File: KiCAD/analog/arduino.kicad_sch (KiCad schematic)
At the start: 53 parts, among them J12 Screw_Terminal_01x04, J13 Screw_Terminal_01x03, J14 Screw_Terminal_01x05, J17 Conn_Coaxial_Small, J18 Conn_Coaxial_Small, J19 Conn_Coaxial_Small, J20 Screw_Terminal_01x04, J21 Screw_Terminal_01x02, J22 Screw_Terminal_01x04, J23 Conn_Coaxial_Small, J24 Conn_Coaxial_Small, J29 Conn_Coaxial_Small, J3 Screw_Terminal_01x04, J30 Conn_Coaxial_Small, J31 8P8C_Shielded, J32 Screw_Terminal_01x02, J6 Screw_Terminal_01x02, J7 Screw_Terminal_01x02, J8 Screw_Terminal_01x02, J9 Screw_Terminal_01x02, Q10 2N7000, Q4 2N7000, Q5 2N7000, Q6 2N7000, Q7 2N7000, U17 Adafruit_PCF8575_Breakout, U18 CD14538B, U3 MCP4728

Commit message: KiCad revC: analog R6 -> 0R jumper (ENC_INT line)
Protoshield already has R7 (330R) + R8 (10K pullup) at the Metro
GPIO input, which is the right place for ESD/noise conditioning
(closest to the sensitive pin). R6 on analog was a duplicate series
resistor on the same signal; dropping it to 0R turns it into an
in-the-path jumper without having to rename the ENC_INT_CLEAN /
ENC_INT labels on multiple sheets.

Co-Authored-By: Claude Opus 4.7 <noreply@anthropic.com>
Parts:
- removed C7: 100nF, Capacitor_THT:C_Disc_D5.0mm_W2.5mm_P5.00mm, symbol Device:C_US
- removed R7: 10K, Resistor_THT:R_Axial_DIN0207_L6.3mm_D2.5mm_P10.16mm_Horizontal, symbol Device:R_US
- R6: value 330R -> 0R

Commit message: revC: accumulated schematic/netlist updates + BOM tooling
- analog + ss_pa netlists regenerated to current schematic state
- interface/arduino/dac/power sheet updates on analog
- fault_shutdown and pa_stage edits on ss_pa (footprint assignments)
- assign_cap_footprints.py: additional VALUE_TO_FOOTPRINT entries
- gen_board_boms.py: per-board BOM generator (multi-sheet .xlsx by
  component category, first-match-wins bucketing, DNP exclusion)
- gen_total_bom.py: consolidated BOM across analog + frontpanel + ss_pa
  for a single Mouser order, board-prefixed references, mixed-footprint
  flagging per Value row

Co-Authored-By: Claude Opus 4.7 <noreply@anthropic.com>
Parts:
- J3: footprint (none) -> TerminalBlock_Phoenix:TerminalBlock_Phoenix_MKDS-1,5-4_1x04_P5.00mm_Horizontal
- J32: footprint (none) -> TerminalBlock_Phoenix:TerminalBlock_Phoenix_MKDS-1,5-2_1x02_P5.00mm_Horizontal
- R12: footprint (none) -> Resistor_THT:R_Axial_DIN0207_L6.3mm_D2.5mm_P10.16mm_Horizontal
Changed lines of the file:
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@@
 			)
 		)
-		(property "Footprint" ""
+		(property "Footprint" "Resistor_THT:R_Axial_DIN0207_L6.3mm_D2.5mm_P10.16mm_Horizontal"
 			(at 207.264 143.764 90)
 			(hide yes)
@@
 			)
 		)
-		(property "Footprint" ""
+		(property "Footprint" "TerminalBlock_Phoenix:TerminalBlock_Phoenix_MKDS-1,5-4_1x04_P5.00mm_Horizontal"
 			(at 24.13 133.35 0)
 			(hide yes)
@@
 			)
 		)
-		(property "Footprint" ""
+		(property "Footprint" "TerminalBlock_Phoenix:TerminalBlock_Phoenix_MKDS-1,5-2_1x02_P5.00mm_Horizontal"
 			(at 215.9 147.32 0)
 			(hide yes)

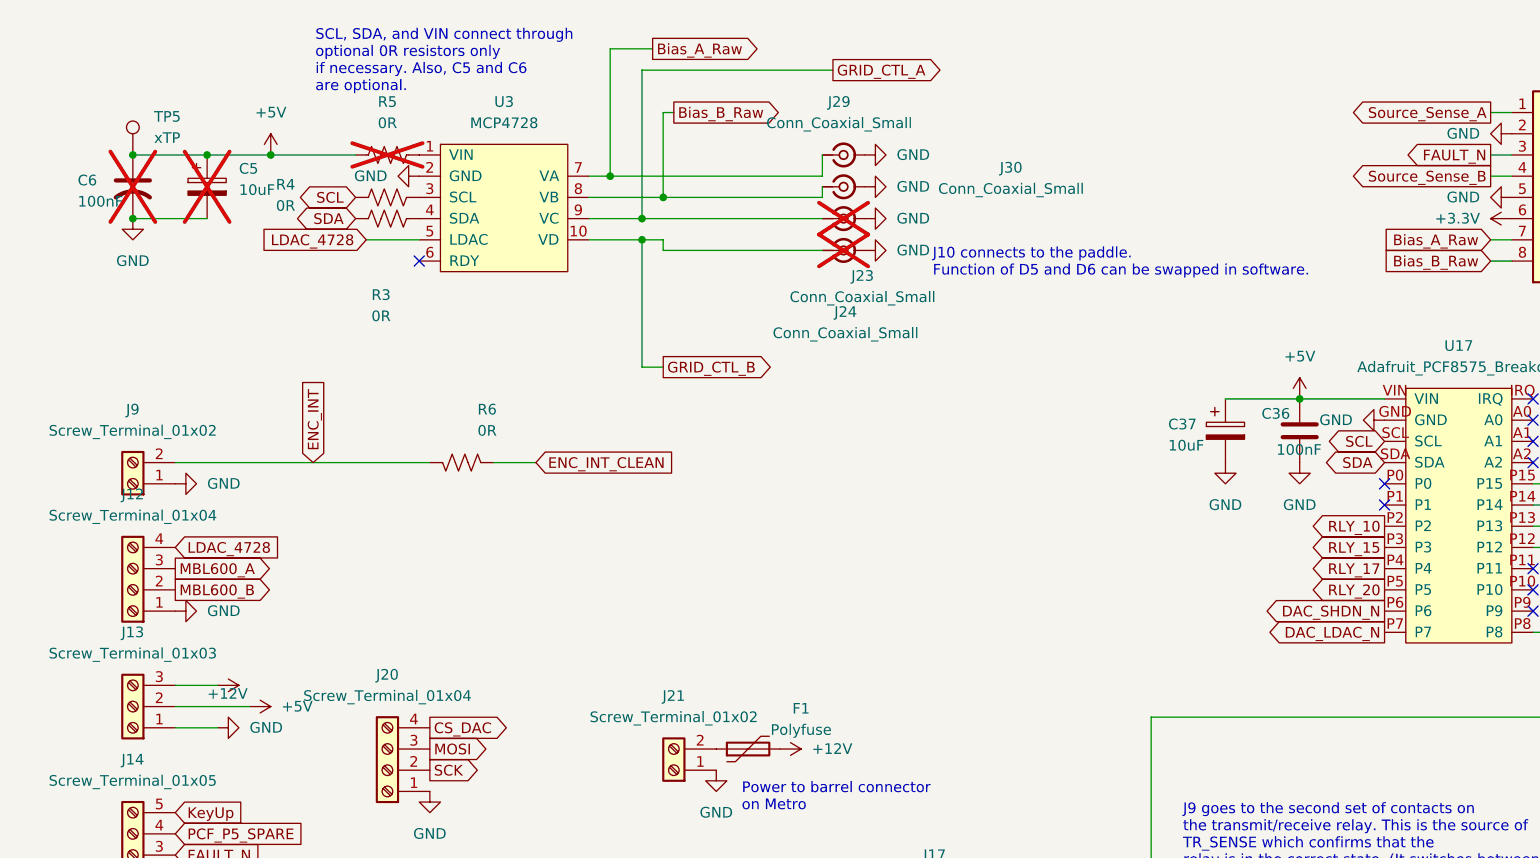
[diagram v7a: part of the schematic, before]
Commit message: revD: analog board — DGFET+RC+buffer chain, LPF moved to ss_pa, PCB resized
Architecture change motivated by the Rev C sim finding that the LM7171
PP driver's +/-12V rails capped clean output at ~4.5W (see commit
3ce203d). Rev D delegates the gain-driver job to an external PA stage
(expected: QRP Labs 10W kit), so the analog board now just:
  Si5351 -> DGFET keyer -> R1(50)+C1(100p) RC @ 32MHz
         -> U1 LM7171 unity-gain follower -> R2(50) back-match -> J1 coax

Analog board changes (vfo_complete.kicad_sch):
  * DELETED: U10, U11, U12 (LM7171 PP driver chain) + feedback R/C,
    AC-coupling caps, V_BIAS network, R_GA/R_GB, C_GA/C_GB, J3/J4
    (dual-ended PP coax outputs)
  * DELETED: U2 reconstruction LPF stage (part of lpf.kicad_sch which
    is now emptied -- content moved to ss_pa/lpf.kicad_sch)
  * ADDED: R1=50R + C1=100pF (32 MHz single-pole RC snubber at the
    DGFET drain), U1 LM7171 unity-gain follower, R2=50R output
    back-match, J1 Conn_Coaxial_Small (new single-ended RF output),
    C2/C3=100nF op-amp bypass caps

Arduino sheet (arduino.kicad_sch):
  * ADDED: J2 Amphenol RJE1D-188 RJ45 for new external LPF board
    - Pins 1,2,3,6: RLY_10/15/17/20 band-select signals from PCF8575
    - Pins 5,8: GRID_CTL_A/B reserved spares for potential future
      tube PA (no other destination on the board, intentional)
    - Pins 4,7,SH: GND
  * ADDED: RLY_40 provision (not yet routed to J2, provision only)
  * T568B wire-pair arrangement for noise immunity

LPF content moved from analog/lpf.kicad_sch -> ss_pa/lpf.kicad_sch
(empty analog LPF sheet remains as a shell; delete later or repurpose).

PCB (analog.kicad_pcb):
  * Resized board outline from oversized 228x178 mm to 200x150 mm
    landscape (300 cm^2 / 46.5 in^2), centered on A3 at (210, 148.5)
  * Four M3 mounting holes H1-H4 placed 5 mm in from each corner
    (hole span 190 x 140 mm)
  * Added "board_only" attribute to each mounting hole so KiCad no
    longer flags them for deletion in Update PCB f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
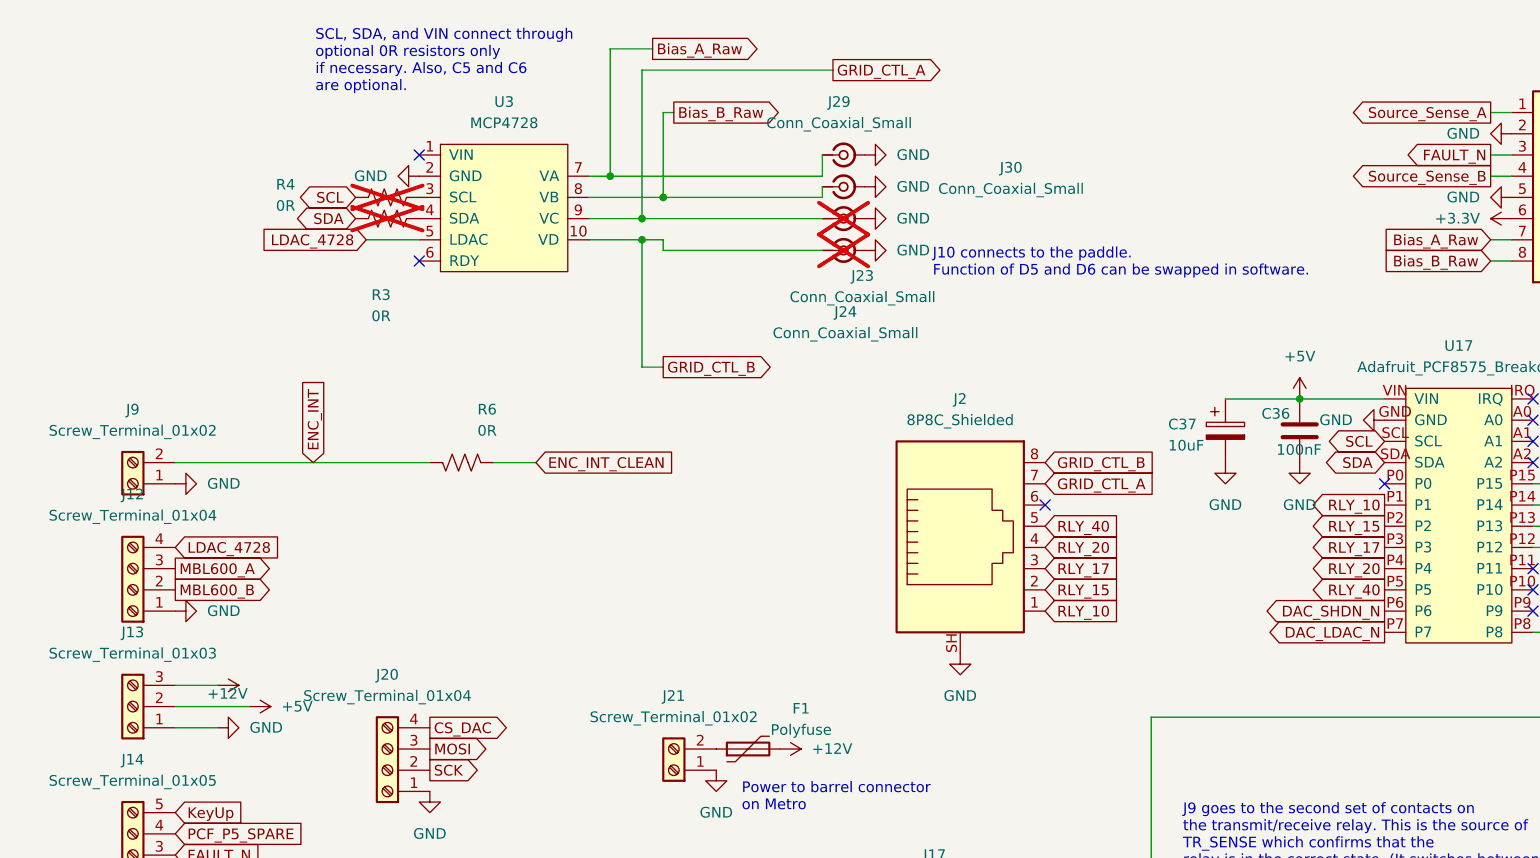
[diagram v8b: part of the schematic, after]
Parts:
- removed C5: 10uF, Capacitor_THT:CP_Radial_D5.0mm_P2.00mm, symbol Device:C_Polarized
- removed C6: 100nF, Capacitor_THT:C_Disc_D5.0mm_W2.5mm_P5.00mm, symbol Device:C_US
- removed R5: 0R, Resistor_THT:R_Axial_DIN0207_L6.3mm_D2.5mm_P10.16mm_Horizontal, symbol Device:R_US
- removed TP5: xTP, Connector_PinHeader_2.54mm:PinHeader_1x01_P2.54mm_Vertical, symbol xmitter:xTP
- added J2: 8P8C_Shielded, xmitter:Amphenol_RJE1D-188_Horizontal_Shielded, symbol Connector:8P8C_Shielded
- R3, R4: now not fitted
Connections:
- net GND: now also J2.SH
- net GRID_CTL_A: now also J2.7
- net GRID_CTL_B: now also J2.8
- net RLY_10: now also U17.P1, J2.1; no longer U17.P2
- net RLY_15: now also U17.P2, J2.2; no longer U17.P3
- net RLY_17: now also U17.P3, J2.3; no longer U17.P4
- net RLY_20: now also U17.P4, J2.4; no longer U17.P5
- new net RLY_40: J2.5, U17.P5
- no-connect marks 14 -> 15
